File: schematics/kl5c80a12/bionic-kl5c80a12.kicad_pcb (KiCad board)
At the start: 2 copper layers, 25.4 x 68.6 mm, 10 parts, among them J1 Bionic-P135, J2 Bionic-P245, U1 KL5C80A12, U2 11AA010-I/TT, U3 74ACT157

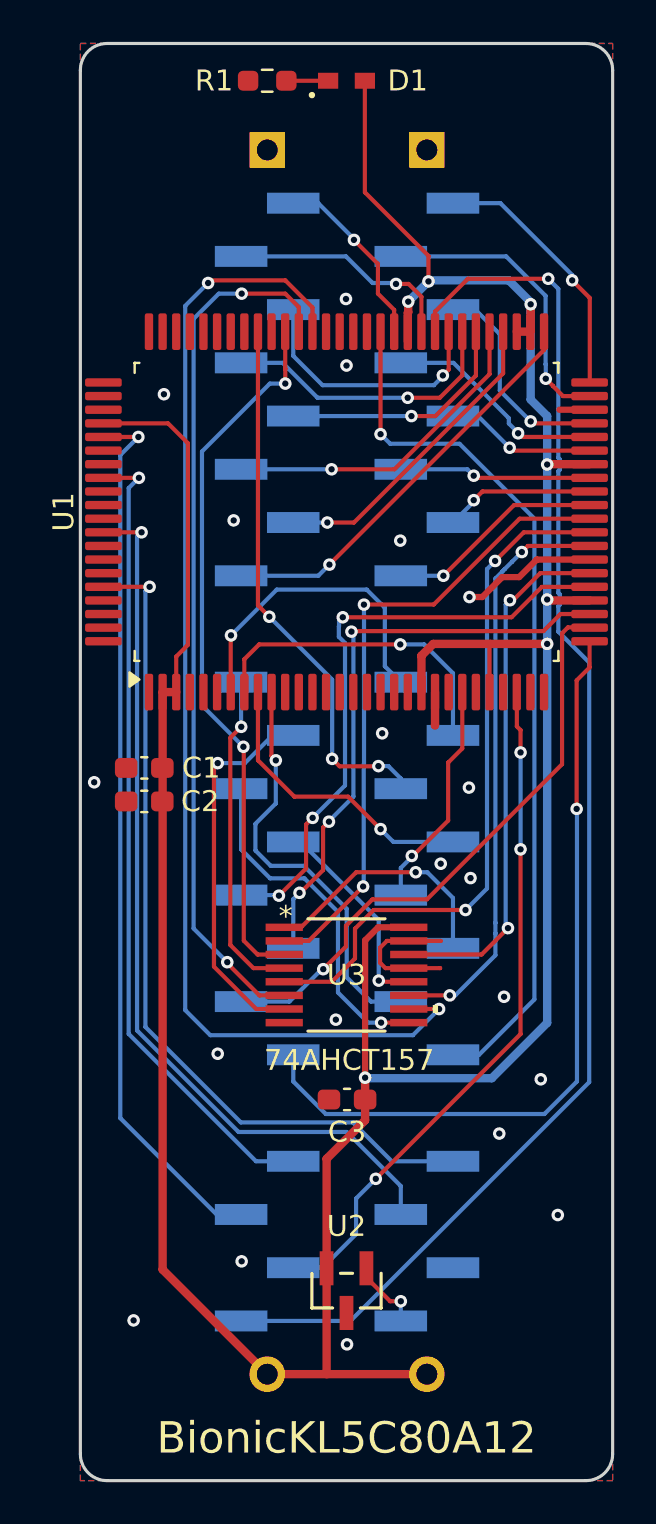
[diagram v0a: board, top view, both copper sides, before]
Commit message: [schematics] Straighten board tracks and regenerate Gerbers
straighten_tracks.py on every routed board: router leftovers snapped to
0/45/90 degrees and redundant segments merged, each pass DRC-checked
(counts unchanged). Gerbers and drill files of the changed boards are
regenerated with each board's plot settings, keeping the committed file
sets; tms9980 keeps its tracks (the rebuild left a dangling VCC stub).
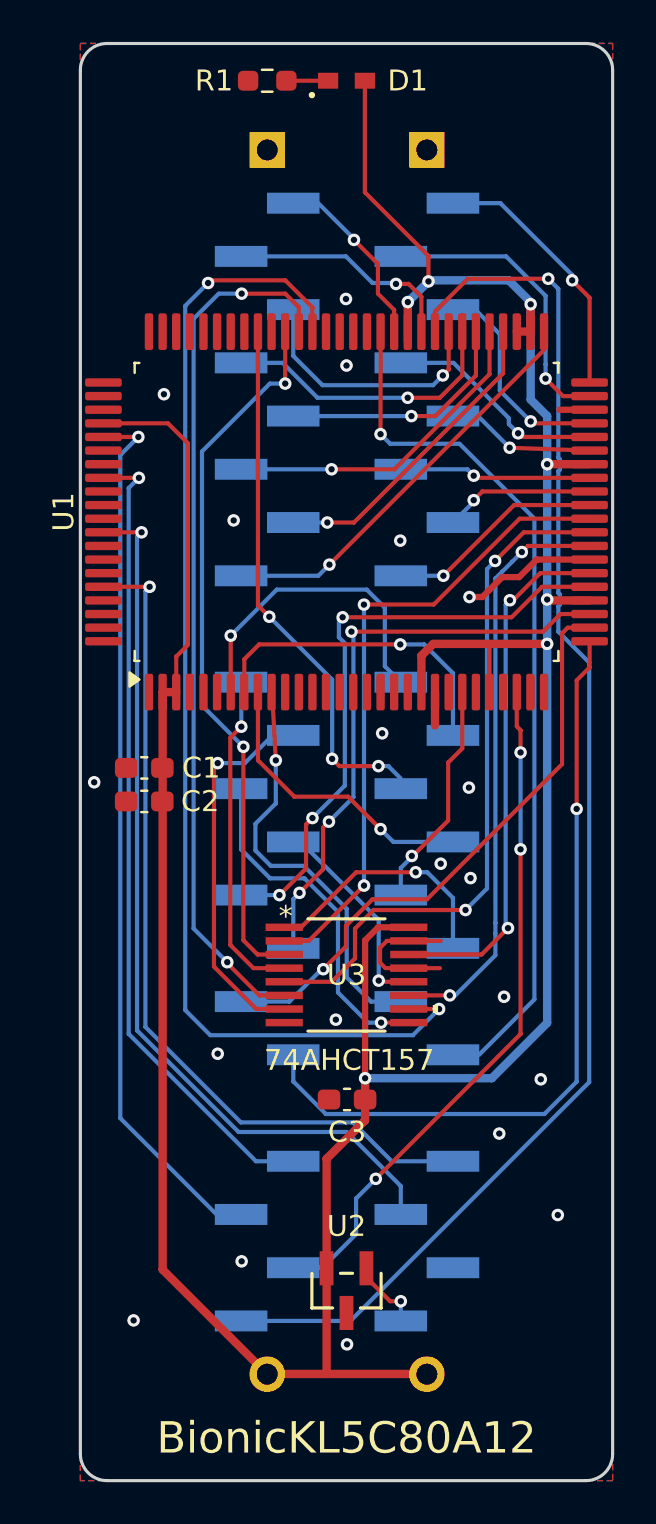
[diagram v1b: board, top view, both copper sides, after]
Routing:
- net A4: track 7.68 -> 5.95 mm
- net XIN: track 41.8 -> 40.6 mm
- net D0: track 8.83 -> 7.63 mm
- net ~{NMI}: track 42.2 -> 41.0 mm
- net A2: track 10.3 -> 9.28 mm
- net P31: track 18.1 -> 17.1 mm
- net D7: track 19.8 -> 18.9 mm
- net ASEL: track 12.1 -> 11.2 mm
- net GND: track 16.9 -> 16.2 mm
- net ERDY: track 32.9 -> 32.3 mm

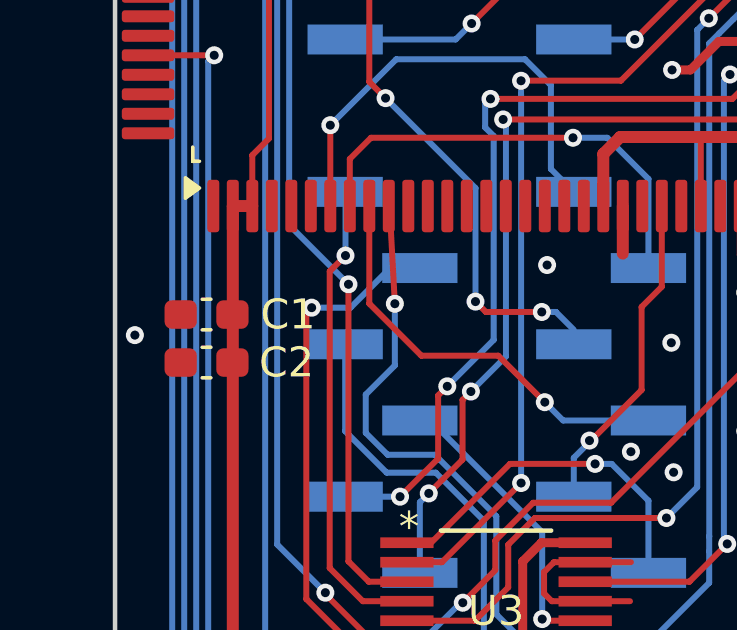
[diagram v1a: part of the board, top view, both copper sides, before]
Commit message: [schematics] Align silkscreen reference labels
align_silk.py snaps each footprint kind's labels onto their common
offset and angle and clears labels DRC flags on silkscreen; 76 labels on
22 boards, no DRC count grows. Their Gerbers are regenerated.
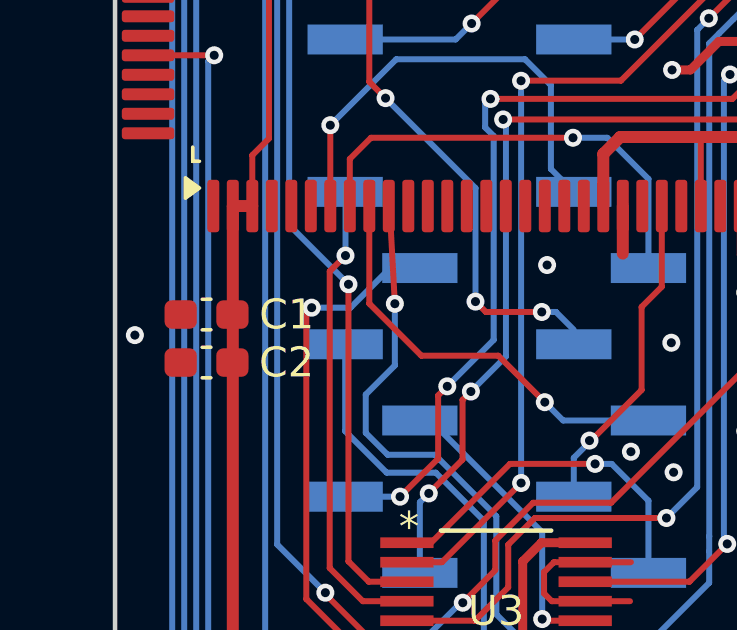
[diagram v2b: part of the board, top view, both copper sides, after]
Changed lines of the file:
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@@
 		(tags "capacitor handsolder")
 		(property "Reference" "C1"
-			(at -2.7156 0 0)
+			(at -2.67 0 0)
 			(layer "F.SilkS")
 			(effects

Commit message: [schematics] Remove the JLC order-number marker from all boards
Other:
- board text removed: "JLCJLCJLCJLC"
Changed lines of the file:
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@@
-		)
-	)
-	(gr_text "JLCJLCJLCJLC"
-		(at 113.7 137.31 0)
-		(layer "B.SilkS")
-		(effects
-			(font
-				(size 0.8 0.8)
-			)
-			(justify bottom mirror)
 		)
 	)
